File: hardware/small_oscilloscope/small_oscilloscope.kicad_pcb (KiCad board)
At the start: 2 copper layers, 98 parts, among them J1 Conn_01x16, J2 Conn_01x16, J3 Conn_Coaxial, J4 Conn_Coaxial, J5 Parellel LCD, J6 Conn_01x02, Q1 NTR5103NT1G, Q2 NTR5103NT1G, Q3 NTR5103NT1G, Q4 NTR5103NT1G, Q5 NTR5103NT1G, Q6 NTR5103NT1G, Q7 NTR5103NT1G, Q8 NTR5103NT1G, Q9 NTR5103NT1G, SW1 SW_MEC_5E, SW2 RotaryEncoder_Switch_MP, SW3 SW_MEC_5E, SW4 SW_MEC_5E, SW5 SW_MEC_5E, SW6 RotaryEncoder_Switch_MP, U1 CH423S, U10 EA2208T6R, U11 FT800Q-T, U12 LM358, U2 TMUX1101DBV, U3 TMUX1101DBV, U4 TMUX1101DBV, U5 TMUX1101DBV, U6 TL084, U7 LM311, U8 LM311, U9 NE555P, Y1 12.0000M

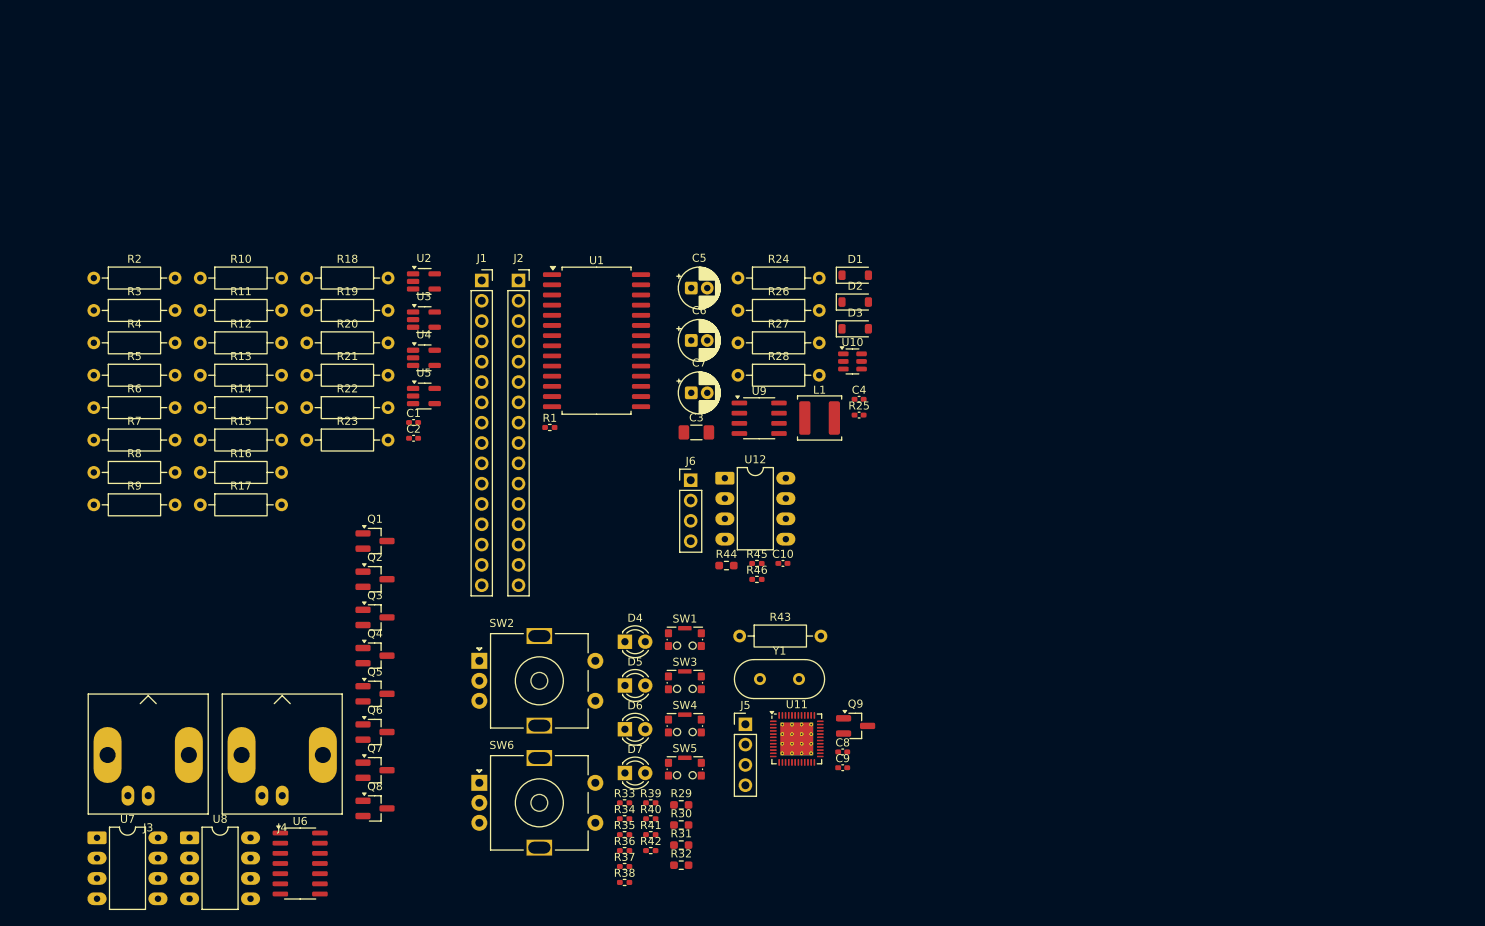
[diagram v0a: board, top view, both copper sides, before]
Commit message: feat: 오실로스코프 회로 설계 업데이트
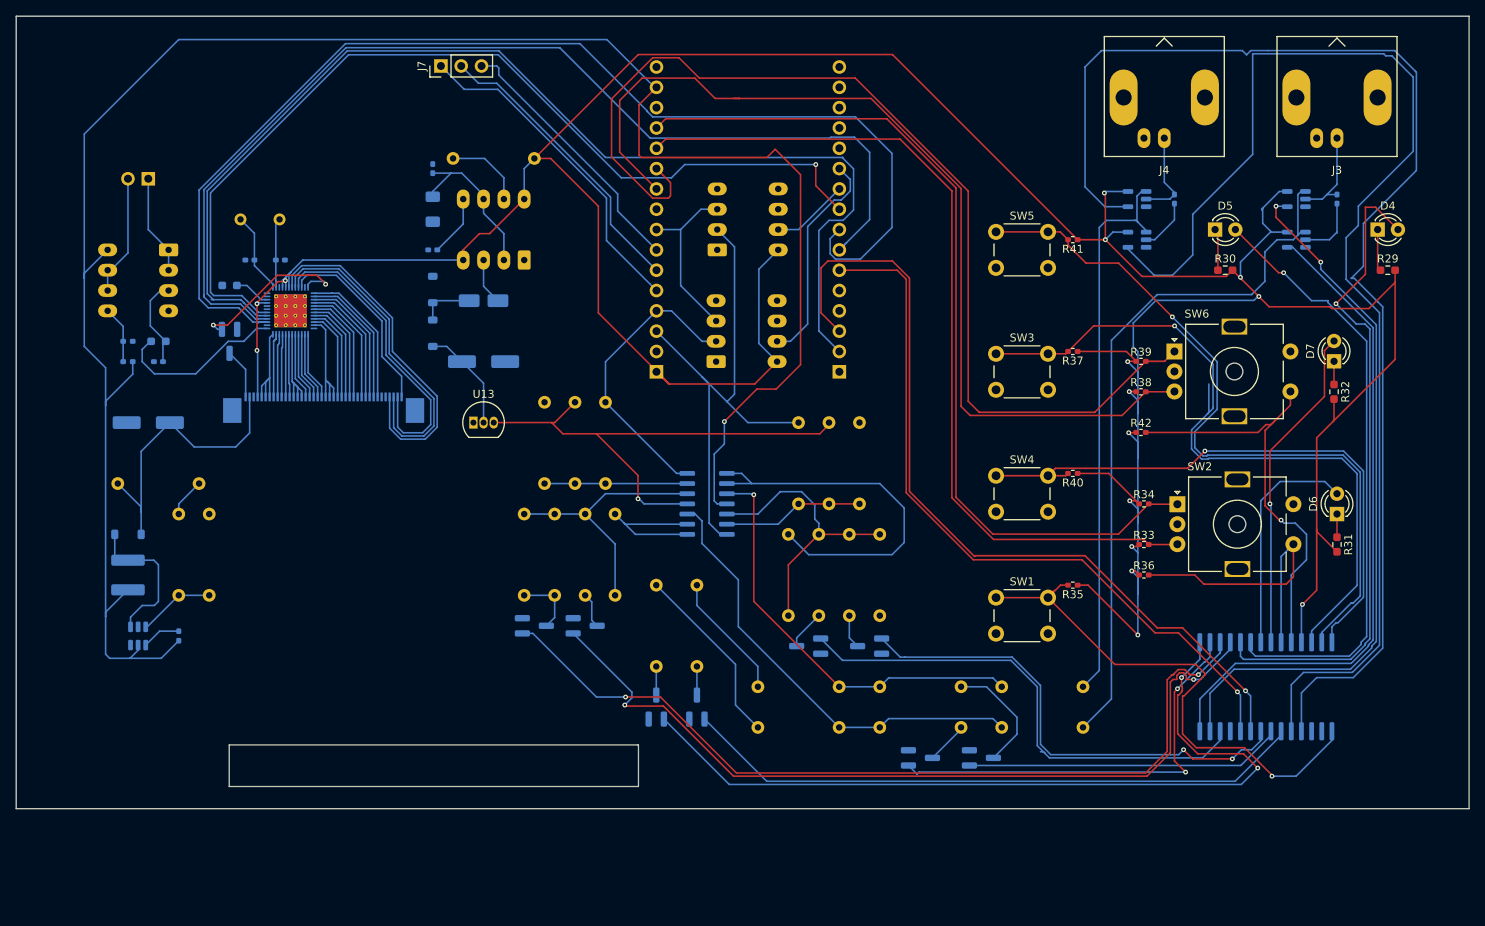
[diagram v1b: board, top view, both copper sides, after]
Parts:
- added J7: Conn_01x03, Connector_PinHeader_2.54mm:PinHeader_1x03_P2.54mm_Vertical, F.Cu at (124.2, 41.8)
- added U13: L79L05_TO92, Package_TO_SOT_THT:TO-92_Inline, F.Cu at (128.3, 86.4)
- C1, C10, C2, C3, C4, C8, C9, D1, D2, D3, J1, J2, L1, Q1, Q2, Q3, Q4, Q5, Q6, Q7, Q8, Q9, R1, R10, R11, R12, R13, R14, R15, R16, R17, R18, R19, R2, R20, R21, R22, R23, R24, R25, R26, R27, R28, R3, R4, R44, R45, R46, R5, R6, R7, R8, R9, U1, U10, U11, U12, U6, U7, U8, Y1: moved to B.Cu
- C5: footprint Capacitor_THT:CP_Radial_D5.0mm_P2.00mm -> Capacitor_SMD:CP_Elec_4x5.7; moved to B.Cu
- C6, C7: footprint Capacitor_THT:CP_Radial_D5.0mm_P2.00mm -> Capacitor_SMD:CP_Elec_6.3x5.7; moved to B.Cu
- J5: footprint Connector_PinHeader_2.54mm:PinHeader_1x04_P2.54mm_Vertical -> Connector_FFC-FPC:TE_4-1734839-0_1x40-1MP_P0.5mm_Horizontal; moved to B.Cu
- J6: footprint Connector_PinHeader_2.54mm:PinHeader_1x04_P2.54mm_Vertical -> Connector_PinHeader_2.54mm:PinHeader_1x02_P2.54mm_Vertical; moved to B.Cu
- R43: value 1K -> 1k; footprint Resistor_THT:R_Axial_DIN0207_L6.3mm_D2.5mm_P10.16mm_Horizontal -> Resistor_SMD:R_0603_1608Metric_Pad0.98x0.95mm_HandSolder; moved to B.Cu
- SW1, SW3, SW4, SW5: footprint Button_Switch_SMD:SW_SPST_CK_KMS2xxGP -> Button_Switch_THT:SW_PUSH_6mm_H4.3mm
- U2, U3, U4, U5: footprint Package_TO_SOT_SMD:SOT-23-5_HandSoldering -> Package_TO_SOT_SMD:SOT-23-5; moved to B.Cu
- U9: footprint Package_SO:SOIC-8_3.9x4.9mm_P1.27mm -> Package_DIP:DIP-8_W7.62mm_LongPads; moved to B.Cu
- moved J3 169.8 mm to (236.2, 50.8)
- moved J4 137.5 mm to (214.6, 50.8)
- moved R2 135.8 mm to (204.5, 124.5), turned to 180 degrees
- moved R4 130.9 mm to (204.5, 119.4), turned to 180 degrees
- moved C1 118.8 mm to (236.2, 58.4), turned to -90 degrees
- moved R3 111.2 mm to (179.1, 124.5)
- moved R29 110.8 mm to (242.6, 67.3)
- moved U3 110.1 mm to (231.1, 58.4), turned to 180 degrees
- moved U2 109.2 mm to (231.1, 63.5), turned to 180 degrees
- moved D4 107.3 mm to (241.3, 62.2)
- moved U7 106.8 mm to (158.8, 64.8)
- moved R5 105.7 mm to (179.1, 119.4)
- moved D7 102.5 mm to (235.8, 78.7), turned to 90 degrees
- moved SW6 102.3 mm to (215.9, 77.5)
- moved R6 101.4 mm to (174.0, 124.5), turned to 180 degrees
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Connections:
- C6 pad 2: -5V -> Net-(D2-A)
- D2 pad 2: -5V -> Net-(D2-A)
- J1 pad 5: unconnected-(J1-34-Pad5) -> Net-(J1-34)
- J1 pad 6: unconnected-(J1-32-Pad6) -> Net-(J1-32)
- J1 pad 7: unconnected-(J1-33-Pad7) -> Net-(J1-33)
- J5 pad 1: Net-(J5-LEDK) -> Net-(J5-YU)
- J5 pad 2: +24V -> Net-(J5-XL)
- J5 pad 3: GND -> Net-(J5-YD)
- J5 pad 4: +3.3V -> Net-(J5-XR)
- R21 pad 2: +5V -> -5V
- R23 pad 2: +5V -> -5V
- SW1 pad 2: /LCD UI/SW3 -> GND
- SW3 pad 2: /LCD UI/SW0 -> GND
- SW4 pad 2: /LCD UI/SW2 -> GND
- SW5 pad 2: /LCD UI/SW1 -> GND
- U10 pad 6: (no net) -> unconnected-(U10-NC-Pad6)
- U11 pad 49: (no net) -> GND
- U11 pad 6: /CS -> /SS
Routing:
- net +3.3V: track 0.00 -> 454.2 mm, vias 0 -> 15
- net +5V: track 0.00 -> 253.7 mm, vias 0 -> 1
- net /Q1: track 0.00 -> 159.5 mm
- net /Q2: track 0.00 -> 155.4 mm
- net /SCK: track 0.00 -> 146.8 mm
- net /MOSI: track 0.00 -> 142.7 mm
- net /MISO: track 0.00 -> 132.5 mm
- net /RE1A: track 0.00 -> 130.4 mm
- net /RE1B: track 0.00 -> 118.9 mm
- net /SS: track 0.00 -> 117.2 mm, vias 0 -> 1
- net /RE0A: track 0.00 -> 111.3 mm
- net /RE0B: track 0.00 -> 109.1 mm
- net /Q11: track 0.00 -> 107.8 mm, vias 0 -> 2
- net /SCL: track 0.00 -> 105.6 mm, vias 0 -> 1
- net /Q12: track 0.00 -> 105.5 mm, vias 0 -> 2
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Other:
- board outline added: 181.6 x 99.1 mm
- board text added: "480 x 272 Monitor"

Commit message: chore: KiCad 프로젝트 백업 파일 정리 및 PCB 파일 업데이트
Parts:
- U13: moved to B.Cu
- moved U13 2.54 mm to (130.8, 86.4), turned to 180 degrees
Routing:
- net GND: track 0.00 -> 46.1 mm, vias 0 -> 24
- net -5V: track 63.8 -> 67.8 mm
- net /LCD UI/SW0: track 91.5 -> 87.7 mm
- net Net-(Q8-D): track 4.24 -> 8.05 mm
- net Net-(U9-DIS): track 10.0 -> 12.8 mm
- net /LCD UI/SW3: track 67.2 -> 65.9 mm
- net /RE1B: track 118.9 -> 118.1 mm
- net /Q6: track 63.1 -> 62.5 mm
- added copper zone on B.Cu, net GND
- added copper zone on F.Cu, net GND

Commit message: feat: 소형 오실로스코프 하드웨어 개발 완료
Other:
- board text added: "4Ohm 3W"
- board text added: "LED0"
- board text added: "LED1"
- board text added: "LINE 0"
- board text added: "LINE 1"
- board text added: "LOLIN D32"
- board text added: "SPEAKER"
- board text added: "Time"
- board text added: "Voltage"
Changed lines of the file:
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@@
 			(outputformat 1)
 			(mirror no)
-			(drillshape 1)
+			(drillshape 0)
 			(scaleselection 1)
-			(outputdirectory "")
+			(outputdirectory "./gerber/")
 		)
 	)
@@
 	)
 	(gr_rect
+		(start 80.75 58.5)
+		(end 186.15 125.65)
+		(stroke
+			(width 0.1)
+			(type default)
+		)
+		(fill no)
+		(layer "F.Mask")
+	)
+	(gr_rect
 		(start 99.15 86.8)
 		(end 119.7 114.8)
@@
 		)
 		(fill no)
-		(layer "F.Mask")
+		(layer "B.Mask")
 	)
 	(gr_rect
@@
 		)
 		(fill no)
-		(layer "F.Mask")
+		(layer "B.Mask")
 	)
 	(gr_rect
-		(start 80.75 58.5)
-		(end 186.15 125.65)
+		(start 148.59 36.068)
+		(end 176.911 84.328)
 		(stroke
 			(width 0.1)
@@
 		)
 		(fill no)
-		(layer "F.Mask")
+		(layer "B.SilkS")
 	)
 	(gr_rect
@@
 		)
 	)
+	(gr_text "Time"
+		(at 221.996 91.059 0)
+		(layer "F.SilkS")
+		(effects
+			(font
+				(size 1 1)
+				(thickness 0.1)
+			)
+			(justify left bottom)
+		)
+	)
+	(gr_text "LINE 0"
+		(at 214.503 57.658 0)
+		(layer "F.SilkS")
+		(effects
+			(font
+				(size 1 1)
+				(thickness 0.1)
+			)
+			(justify bottom)
+		)
+	)
+	(gr_text "SPEAKER"
+		(at 83.312 52.832 0)
+		(layer "F.SilkS")
+		(effects
+			(font
+				(size 1 1)
+				(thickness 0.1)
+			)
+			(justify left bottom)
+		)
+	)
+	(gr_text "4Ohm 3W"
+		(at 82.804 50.546 0)
+		(layer "F.SilkS")
+		(effects
+			(font
+				(size 1 1)
+				(thickness 0.1)
+			)
+			(justify left bottom)
+		)
+	)
+	(gr_text "LINE 1"
+		(at 234.823 57.531 0)
+		(layer "F.SilkS")
+		(effects
+			(font
+				(size 1 1)
+				(thickness 0.1)
+			)
+			(justify left bottom)
+		)
+	)
+	(gr_text "LED1"
+		(at 215.265 62.992 0)
+		(layer "F.SilkS")
+		(effects
+			(font
+				(size 1 1)
+				(thickness 0.1)
+			)
+			(justify left bottom)
+		)
+	)
+	(gr_text "Voltage"
+		(at 220.853 72.009 0)
+		(layer "F.SilkS")
+		(effects
+			(font
+				(size 1 1)
+				(thickness 0.1)
+			)
+			(justify left bottom)
+		)
+	)
+	(gr_text "LED0"
+		(at 235.712 63.31 0)
+		(layer "F.SilkS")
+		(effects
+			(font
+				(size 1 1)
+				(thickness 0.1)
+			)
+			(justify left bottom)
+		)
+	)
+	(gr_text "LOLIN D32"
+		(at 166.624 38.862 0)
+		(layer "B.SilkS")
+		(effects
+			(font
+				(size 1 1)
+				(thickness 0.1)
+			)
+			(justify left bottom mirror)
+		)
+	)
 	(segment
 		(start 232.49 63.5)
@@
 	)
 	(segment
-		(start 109.093 74.803)
-		(end 109.22 74.93)
-		(width 0.2)
-		(layer "B.Cu")
-		(net 6)
-	)
-	(segment
-		(start 107.7439 68.346)
+		(start 107.676 68.346)
 		(end 110.256 68.346)
 		(width 0.2)
@@
 	)
 	(segment
-		(start 107.21 68.812)
-		(end 107.569 68.453)
-		(width 0.2)
-		(layer "B.Cu")
-		(net 6)
-	)
-	(segment
 		(start 88.3325 78.0455)
 		(end 87.884 77.597)
@@
 	)
 	(segment
-		(start 107.676 68.346)
-		(end 107.7439 68.346)
-		(width 0.2)
-		(layer "B.Cu")
-		(net 6)
-	)
-	(segment
 		(start 86.36 111.8925)
 		(end 86.36 111.230001)
@@
 	)
 	(segment
-		(start 101.6853 74.19)
-		(end 101.578 74.19)
-		(width 0.2)
-		(layer "B.Cu")
-		(net 6)
-	)
-	(segment
 		(start 100.8 83.15)
 		(end 100.8 85.179)
@@
 	)
 	(segment
-		(start 107.569 68.453)
+		(start 107.21 68.812)
 		(end 107.676 68.346)
 		(width 0.2)
@@
 	)
 	(segment
-		(start 102.4725 74.19)
-		(end 101.6853 74.19)
+		(start 101.578 74.19)
+		(end 102.4725 74.19)
 		(width 0.2)
 		(layer "B.Cu")
@@
 	)
 	(segment
-		(start 101.6853 74.19)
-		(end 101.854 74.19)
-		(width 0.2)
-		(layer "B.Cu")
-		(net 6)
-	)
-	(segment
 		(start 109.22 74.93)
 		(end 109.22 75.565)
@@
 	(segment
 		(start 108.88 74.59)
-		(end 109.093 74.803)
+		(end 109.22 74.93)
 		(width 0.2)
 		(layer "B.Cu")
@@
 	)
 	(segment
-		(start 237.363 68.453)
-		(end 237.363 64.778767)
-		(width 0.2)
-		(layer "B.Cu")
-		(net 101)
-	)
-	(segment
 		(start 242.316 40.513)
 		(end 242.062 40.259)
@@
 	)
 	(segment
-		(start 237.363 64.652498)
-		(end 237.363 60.833)
-		(width 0.2)
-		(layer "B.Cu")
-		(net 101)
-	)
-	(segment
 		(start 237.363 60.833)
 		(end 245.745 52.451)
@@
 	)
 	(segment
-		(start 237.363 64.778767)
-		(end 237.363 64.652498)
+		(start 237.363 68.453)
+		(end 237.363 60.833)
 		(width 0.2)
 		(layer "B.Cu")

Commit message: board edit
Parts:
- added REF**: TestPoint_Plated_Hole_D3.0mm, TestPoint:TestPoint_Plated_Hole_D3.0mm, F.Cu at (248.0, 41.0)
- added REF**: TestPoint_Plated_Hole_D3.0mm, TestPoint:TestPoint_Plated_Hole_D3.0mm, F.Cu at (77.0, 41.0)
- added REF**: TestPoint_Plated_Hole_D3.0mm, TestPoint:TestPoint_Plated_Hole_D3.0mm, F.Cu at (77.0, 129.0)
- added REF**: TestPoint_Plated_Hole_D3.0mm, TestPoint:TestPoint_Plated_Hole_D3.0mm, F.Cu at (248.0, 129.0)
- U11: footprint Package_DFN_QFN:VQFN-48-1EP_6x6mm_P0.4mm_EP4.1x4.1mm_ThermalVias -> Package_DFN_QFN:VQFN-48-1EP_7x7mm_P0.5mm_EP4.1x4.1mm
- moved D6 2.79 mm to (236.2, 95.0), turned to -90 degrees
- moved D5 2.54 mm to (223.5, 62.2), turned to 180 degrees
- moved D4 2.54 mm to (243.8, 62.2), turned to 180 degrees
- moved D7 2.50 mm to (235.8, 76.2), turned to -90 degrees
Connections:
- D4 pad 1: Net-(D4-K) -> /LCD UI/LED0
- D4 pad 2: /LCD UI/LED0 -> Net-(D4-A)
- D5 pad 1: Net-(D5-K) -> /LCD UI/LED1
- D5 pad 2: /LCD UI/LED1 -> Net-(D5-A)
- D6 pad 1: Net-(D6-K) -> /LCD UI/LEDRE0
- D6 pad 2: /LCD UI/LEDRE0 -> Net-(D6-A)
- D7 pad 1: Net-(D7-K) -> /LCD UI/LEDRE1
- D7 pad 2: /LCD UI/LEDRE1 -> Net-(D7-A)
- R29 pad 1: Net-(D4-K) -> Net-(D4-A)
- R30 pad 1: Net-(D5-K) -> Net-(D5-A)
- R31 pad 1: Net-(D6-K) -> Net-(D6-A)
- R32 pad 1: Net-(D7-K) -> Net-(D7-A)
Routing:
- net Net-(D5-K): track 5.23 -> 0.00 mm
- net Net-(D5-A): track 0.00 -> 5.23 mm
- net Net-(D4-K): track 5.23 -> 0.00 mm
- net Net-(D4-A): track 0.00 -> 5.23 mm
- net Net-(D7-K): track 2.90 -> 0.00 mm
- net Net-(D7-A): track 0.00 -> 2.90 mm
- net Net-(D6-K): track 2.90 -> 0.00 mm
- net Net-(D6-A): track 0.00 -> 2.90 mm
- net GND: track 46.0 -> 43.5 mm
- net /SCK: track 146.6 -> 145.2 mm
- net Net-(J5-R3): track 8.44 -> 7.38 mm
- net Net-(J5-R0): track 13.2 -> 12.3 mm
- net Net-(J5-G0): track 12.3 -> 11.5 mm
- net /Q1: track 159.2 -> 158.4 mm
- net Net-(J5-G7): track 8.52 -> 7.79 mm
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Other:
- outline, holes or cut-outs redrawn
- board text added: "Small Oscilliscope made by Giho Park"

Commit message: oscilliscope first success
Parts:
- removed the C3 at (123.2, 59.7)
- removed the C4 at (123.2, 64.8)
- removed the C6 at (129.5, 78.7)
- removed the D2 at (123.2, 75.2)
- removed the J2 at (174.0, 80.0)
- removed the Q9 at (97.8, 76.2)
- removed the R25 at (123.2, 54.6)
- removed the R27 at (91.4, 97.8)
- removed the REF** at (248.0, 41.0)
- removed the REF** at (77.0, 41.0)
- removed the REF** at (77.0, 129.0)
- removed the REF** at (248.0, 129.0)
- removed the U13 at (130.8, 86.4)
- removed the U3 at (231.1, 58.4)
- removed the U4 at (211.2, 63.5)
- removed the U5 at (211.2, 58.4)
- added AE1: Antenna_Chip, Inductor_SMD:L_1206_3216Metric_Pad1.22x1.90mm_HandSolder, B.Cu at (173.7, 130.4)
- added C1: 10u, Capacitor_SMD:CP_Elec_5x5.3, B.Cu at (161.3, 104.4)
- added C10: 10u, Capacitor_SMD:CP_Elec_6.3x5.7, B.Cu at (146.3, 99.6)
- added C13: 10u, Capacitor_SMD:CP_Elec_5x5.3, B.Cu at (110.0, 63.5)
- added C2: 0.1u, Capacitor_SMD:C_0402_1005Metric_Pad0.74x0.62mm_HandSolder, B.Cu at (179.4, 115.8)
- added C7: 47u, Capacitor_SMD:CP_Elec_5x5.3, B.Cu at (140.5, 105.4)
- added C8: 100u, Capacitor_SMD:CP_Elec_5x5.3, B.Cu at (128.5, 104.6)
- added C9: 47u, Capacitor_SMD:CP_Elec_6.3x5.7, B.Cu at (135.4, 98.3)
- added D12: LED, LED_THT:LED_D3.0mm, F.Cu at (115.2, 47.0)
- added D3: 1N5819, Diode_SMD:D_SOD-123, B.Cu at (142.0, 93.5)
- added D4: LED_Small, LED_THT:LED_D3.0mm, F.Cu at (99.7, 47.0)
- added D5: LED_Small, LED_THT:LED_D3.0mm, F.Cu at (107.6, 47.0)
- added D6: 1N5819, Diode_SMD:D_SOD-123, B.Cu at (130.3, 91.2)
- added D7: 1N5819, Diode_SMD:D_SOD-123, B.Cu at (148.1, 69.1)
- added J4: BAT, Connector_PinSocket_2.54mm:PinSocket_1x02_P2.54mm_Vertical, F.Cu at (79.3, 50.3)
- added K1: FINDER-40.41, Relay_THT:Relay_SPDT_Finder_40.41, F.Cu at (205.9, 81.5)
- added K2: FINDER-40.41, Relay_THT:Relay_SPDT_Finder_40.41, F.Cu at (233.2, 81.5)
- added K3: FINDER-40.41, Relay_THT:Relay_SPDT_Finder_40.41, F.Cu at (219.5, 81.5)
- added K4: FINDER-40.41, Relay_THT:Relay_SPDT_Finder_40.41, F.Cu at (233.2, 120.6)
- added L2: 10u, Inductor_SMD:L_7.3x7.3_H3.5, B.Cu at (140.2, 86.4)
- added L3: 10u, Inductor_SMD:L_7.3x7.3_H3.5, B.Cu at (129.8, 85.1)
- added L4: 10u, Inductor_SMD:L_7.3x7.3_H3.5, B.Cu at (136.4, 75.7)
- added L5: 100u, Inductor_SMD:L_7.3x7.3_H3.5, B.Cu at (149.9, 75.4)
- added Q1: 2SC4671, Package_TO_SOT_SMD:SOT-523, B.Cu at (88.8, 47.5)
- added Q12: 2SC4671, Package_TO_SOT_SMD:SOT-523, F.Cu at (233.7, 125.5)
- added Q13: 2SC4671, Package_TO_SOT_SMD:SOT-523, B.Cu at (91.3, 116.8)
- added Q14: 2SC4671, Package_TO_SOT_SMD:SOT-523, F.Cu at (119.4, 51.7)
- added Q15: 2SC4671, Package_TO_SOT_SMD:SOT-523, F.Cu at (119.4, 54.9)
- added Q7: 2SC4671, Package_TO_SOT_SMD:SOT-523, F.Cu at (235.3, 90.8)
- added Q8: 2SC4671, Package_TO_SOT_SMD:SOT-523, F.Cu at (222.8, 90.7)
- added R10: 10k, Resistor_SMD:R_0402_1005Metric_Pad0.72x0.64mm_HandSolder, B.Cu at (85.5, 45.5)
- added R11: 10k, Resistor_SMD:R_0402_1005Metric_Pad0.72x0.64mm_HandSolder, B.Cu at (85.5, 50.3)
- added R12: 10K, Resistor_SMD:R_0402_1005Metric_Pad0.72x0.64mm_HandSolder, B.Cu at (156.2, 109.2)
- added R13: 100, Resistor_SMD:R_0603_1608Metric_Pad0.98x0.95mm_HandSolder, B.Cu at (152.4, 106.7)
- added R14: 10K, Resistor_SMD:R_0402_1005Metric_Pad0.72x0.64mm_HandSolder, B.Cu at (149.9, 113.3)
- added R15: 10K, Resistor_SMD:R_0402_1005Metric_Pad0.72x0.64mm_HandSolder, B.Cu at (149.9, 111.8)
- added R16: 4K7, Resistor_SMD:R_0402_1005Metric_Pad0.72x0.64mm_HandSolder, B.Cu at (149.9, 109.0)
- added R17: 10K, Resistor_SMD:R_0402_1005Metric_Pad0.72x0.64mm_HandSolder, B.Cu at (149.9, 110.2)
- added R18: 10K, Resistor_SMD:R_0402_1005Metric_Pad0.72x0.64mm_HandSolder, B.Cu at (152.7, 113.3)
- added R19: 3K, Resistor_SMD:R_0402_1005Metric_Pad0.72x0.64mm_HandSolder, B.Cu at (152.7, 111.8)
- added R2: 10k, Resistor_SMD:R_0402_1005Metric_Pad0.72x0.64mm_HandSolder, B.Cu at (187.2, 125.1)
- added R20: 820R, Resistor_SMD:R_0402_1005Metric_Pad0.72x0.64mm_HandSolder, B.Cu at (152.7, 109.0)
- added R22: 10K, Resistor_SMD:R_0402_1005Metric_Pad0.72x0.64mm_HandSolder, B.Cu at (158.8, 109.2)
- added R23: 1k, Resistor_SMD:R_0603_1608Metric_Pad0.98x0.95mm_HandSolder, F.Cu at (139.3, 45.7)
- added R3: 10k, Resistor_SMD:R_0402_1005Metric_Pad0.72x0.64mm_HandSolder, B.Cu at (170.2, 121.8)
- added R33: 3k, Resistor_SMD:R_0402_1005Metric_Pad0.72x0.64mm_HandSolder, F.Cu at (201.5, 86.4)
- added R35: 3K6, Resistor_THT:R_Axial_DIN0207_L6.3mm_D2.5mm_P10.16mm_Horizontal, B.Cu at (175.0, 63.8)
- added R38: 3k, Resistor_SMD:R_0402_1005Metric_Pad0.72x0.64mm_HandSolder, F.Cu at (232.2, 90.9)
- added R4: 10k, Resistor_SMD:R_0402_1005Metric_Pad0.72x0.64mm_HandSolder, B.Cu at (163.7, 113.3)
- added R42: 3K6, Resistor_THT:R_Axial_DIN0207_L6.3mm_D2.5mm_P10.16mm_Horizontal, B.Cu at (159.0, 65.9)
- added R43: 3K6, Resistor_THT:R_Axial_DIN0207_L6.3mm_D2.5mm_P10.16mm_Horizontal, B.Cu at (155.2, 65.9)
- added R5: 10k, Resistor_SMD:R_0402_1005Metric_Pad0.72x0.64mm_HandSolder, B.Cu at (169.3, 107.2)
- added R51: 3k, Resistor_SMD:R_0402_1005Metric_Pad0.72x0.64mm_HandSolder, F.Cu at (220.5, 90.7)
- added R52: 3k, Resistor_SMD:R_0402_1005Metric_Pad0.72x0.64mm_HandSolder, F.Cu at (231.0, 125.6)
- added R54: 10k, Resistor_SMD:R_0402_1005Metric_Pad0.72x0.64mm_HandSolder, B.Cu at (88.0, 119.9)
- added R56: 10k, Resistor_SMD:R_0402_1005Metric_Pad0.72x0.64mm_HandSolder, B.Cu at (90.8, 120.1)
- added R57: 147k, Resistor_SMD:R_0402_1005Metric_Pad0.72x0.64mm_HandSolder, B.Cu at (142.2, 80.5)
- added R58: 1k, Resistor_SMD:R_0603_1608Metric_Pad0.98x0.95mm_HandSolder, F.Cu at (101.2, 51.6)
- added R59: 1k, Resistor_SMD:R_0603_1608Metric_Pad0.98x0.95mm_HandSolder, F.Cu at (109.1, 51.6)
- added R6: 10k, Resistor_SMD:R_0402_1005Metric_Pad0.72x0.64mm_HandSolder, B.Cu at (169.3, 108.5)
- added R60: 7.5k, Resistor_SMD:R_1206_3216Metric_Pad1.30x1.75mm_HandSolder, B.Cu at (142.5, 71.1)
- added R61: 1k, Resistor_SMD:R_0603_1608Metric_Pad0.98x0.95mm_HandSolder, F.Cu at (85.8, 45.2)
- added R62: 22k, Resistor_SMD:R_1206_3216Metric_Pad1.30x1.75mm_HandSolder, B.Cu at (124.2, 74.2)
- added R63: 470k, Resistor_SMD:R_0402_1005Metric_Pad0.72x0.64mm_HandSolder, B.Cu at (136.9, 62.5)
- added R64: 3k, Resistor_SMD:R_0402_1005Metric_Pad0.72x0.64mm_HandSolder, B.Cu at (124.5, 68.6)
- added R65: 100k, Resistor_SMD:R_0402_1005Metric_Pad0.72x0.64mm_HandSolder, B.Cu at (133.6, 62.5)
- added R7: 10k, Resistor_SMD:R_0402_1005Metric_Pad0.72x0.64mm_HandSolder, B.Cu at (173.5, 107.6)
- added R8: 10k, Resistor_SMD:R_0402_1005Metric_Pad0.72x0.64mm_HandSolder, B.Cu at (85.5, 48.0)
- added R80: 150, Resistor_SMD:R_0402_1005Metric_Pad0.72x0.64mm_HandSolder, B.Cu at (94.2, 79.8)
- added R81: 10k, Resistor_SMD:R_0402_1005Metric_Pad0.72x0.64mm_HandSolder, B.Cu at (93.0, 74.2)
- added R82: 10k, Resistor_SMD:R_0402_1005Metric_Pad0.72x0.64mm_HandSolder, B.Cu at (94.2, 70.1)
- added R83: 10R, Resistor_SMD:R_1206_3216Metric_Pad1.30x1.75mm_HandSolder, B.Cu at (87.4, 77.2)
- added R84: 10R, Resistor_SMD:R_1206_3216Metric_Pad1.30x1.75mm_HandSolder, B.Cu at (87.4, 74.4)
- added R85: 10R, Resistor_SMD:R_1206_3216Metric_Pad1.30x1.75mm_HandSolder, B.Cu at (87.4, 71.9)
- added R86: 10R, Resistor_SMD:R_1206_3216Metric_Pad1.30x1.75mm_HandSolder, B.Cu at (94.0, 75.9)
- added R87: 10R, Resistor_SMD:R_1206_3216Metric_Pad1.30x1.75mm_HandSolder, B.Cu at (94.0, 72.1)
- added R9: 10k, Resistor_SMD:R_0402_1005Metric_Pad0.72x0.64mm_HandSolder, B.Cu at (85.5, 52.8)
- added R93: 3k, Resistor_SMD:R_0402_1005Metric_Pad0.72x0.64mm_HandSolder, F.Cu at (116.6, 51.6)
- added R94: 10k, Resistor_SMD:R_0402_1005Metric_Pad0.72x0.64mm_HandSolder, F.Cu at (123.3, 54.2)
- added R95: 10k, Resistor_SMD:R_0402_1005Metric_Pad0.72x0.64mm_HandSolder, F.Cu at (123.3, 52.5)
- added REF**: TestPoint_Loop_D3.80mm_Drill2.8mm, TestPoint:TestPoint_Loop_D3.80mm_Drill2.8mm, F.Cu at (245.0, 44.0)
- added REF**: TestPoint_Loop_D3.80mm_Drill2.8mm, TestPoint:TestPoint_Loop_D3.80mm_Drill2.8mm, F.Cu at (245.0, 134.0)
- added REF**: TestPoint_Loop_D3.80mm_Drill2.8mm, TestPoint:TestPoint_Loop_D3.80mm_Drill2.8mm, F.Cu at (77.0, 134.0)
- added REF**: TestPoint_Loop_D3.80mm_Drill2.8mm, TestPoint:TestPoint_Loop_D3.80mm_Drill2.8mm, F.Cu at (77.0, 44.0)
- added U10: EA8105, Package_TO_SOT_SMD:SOT-23-6, B.Cu at (136.4, 66.0)
- added U11: LM2576S-12, Package_TO_SOT_SMD:TO-263-5_TabPin3, B.Cu at (145.5, 55.0)
- added U14: CH340C, Package_SO:SOIC-16_3.9x9.9mm_P1.27mm, F.Cu at (132.3, 54.5)
- added U7: EA2208T6R, Package_TO_SOT_SMD:SOT-23-6, B.Cu at (142.7, 76.5)
- added U8: TP4056-42-ESOP8, Package_SO:SOIC-8-1EP_3.9x4.9mm_P1.27mm_EP2.41x3.3mm_ThermalVias, F.Cu at (92.7, 47.8)
- C5: value 10u -> 100u; footprint Capacitor_SMD:CP_Elec_4x5.7 -> Capacitor_SMD:CP_Elec_5x5.3
- C6: renamed from C7; value 47u -> 10u; footprint Capacitor_SMD:CP_Elec_6.3x5.7 -> Capacitor_SMD:CP_Elec_5x5.3
- D1: value D_Schottky -> 1N5225B; footprint Diode_SMD:D_SOD-123 -> Diode_THT:D_A-405_P7.62mm_Horizontal
- J1: value Conn_01x16 -> SIGNAL; footprint Connector_PinSocket_2.54mm:PinSocket_1x16_P2.54mm_Vertical -> Connector_PinSocket_2.54mm:PinSocket_1x02_P2.54mm_Vertical
- J6: value Conn_01x02 -> SPEAKER; footprint Connector_PinHeader_2.54mm:PinHeader_1x02_P2.54mm_Vertical -> Connector_PinSocket_2.54mm:PinSocket_1x02_P2.54mm_Vertical
- J7: value Conn_01x03 -> USB_B_Mini; footprint Connector_PinHeader_2.54mm:PinHeader_1x03_P2.54mm_Vertical -> Connector_USB:USB_Mini-B_Lumberg_2486_01_Horizontal
- L1: value 1u -> 10u; footprint Inductor_SMD:L_Changjiang_FNR5045S -> Inductor_SMD:L_7.3x7.3_H3.5
- Q10: renamed from Q5; value NTR5103NT1G -> BSS138
- Q11: renamed from Q7; value NTR5103NT1G -> BSS138
- Q2: value NTR5103NT1G -> 2SC4671; footprint Package_TO_SOT_SMD:SOT-23_Handsoldering -> Package_TO_SOT_SMD:SOT-523
- Q3: value NTR5103NT1G -> 2SC4671; footprint Package_TO_SOT_SMD:SOT-23_Handsoldering -> Package_TO_SOT_SMD:SOT-523; moved to F.Cu
- Q4: value NTR5103NT1G -> BSS138; moved to F.Cu
- Q5: renamed from Q6; value NTR5103NT1G -> BSS138
- Q6: renamed from Q8; value NTR5103NT1G -> BSS138
- Q9: renamed from Q1; value NTR5103NT1G -> BSS138; moved to F.Cu
- R21: value 3K -> 10K; footprint Resistor_THT:R_Axial_DIN0207_L6.3mm_D2.5mm_P10.16mm_Horizontal -> Resistor_SMD:R_0402_1005Metric_Pad0.72x0.64mm_HandSolder
- R24: value 560 -> 1k; footprint Resistor_THT:R_Axial_DIN0207_L6.3mm_D2.5mm_P10.16mm_Horizontal -> Resistor_SMD:R_0603_1608Metric_Pad0.98x0.95mm_HandSolder; moved to F.Cu
- R27: renamed from R5; moved to F.Cu
- R30: renamed from R15; value 500 -> 500R
- R31: renamed from R17; value 500 -> 500R
- R36: renamed from R23; value 3K -> 3K6
- R37: renamed from R19; value 150 -> 150R
- R44: renamed from R3; moved to F.Cu
- R47: renamed from R14; value 500 -> 500R
- R48: renamed from R16; value 500 -> 500R
- R49: renamed from R18; value 150 -> 150R
- R53: renamed from R26; value 10k -> 4.7k; footprint Resistor_THT:R_Axial_DIN0207_L6.3mm_D2.5mm_P10.16mm_Horizontal -> Resistor_SMD:R_0402_1005Metric_Pad0.72x0.64mm_HandSolder
- R55: renamed from R28; value 500 -> 120; footprint Resistor_THT:R_Axial_DIN0207_L6.3mm_D2.5mm_P10.16mm_Horizontal -> Resistor_SMD:R_0402_1005Metric_Pad0.72x0.64mm_HandSolder
- R89: renamed from R43; value 1k -> 10k; footprint Resistor_SMD:R_0603_1608Metric_Pad0.98x0.95mm_HandSolder -> Resistor_SMD:R_0402_1005Metric_Pad0.72x0.64mm_HandSolder
- U1: moved to F.Cu
- U13: renamed from U12; footprint Package_DIP:DIP-8_W7.62mm_LongPads -> Package_SO:SOIC-8_3.9x4.9mm_P1.27mm
- U2: value TMUX1101DBV -> ESP32-PICO-D4; footprint Package_TO_SOT_SMD:SOT-23-5 -> Package_DFN_QFN:QFN-48-1EP_7x7mm_P0.5mm_EP5.3x5.3mm
- U4: renamed from U7; moved to F.Cu
- U5: renamed from U8; moved to F.Cu
- U9: value NE555P -> EA2208T6R; footprint Package_DIP:DIP-8_W7.62mm_LongPads -> Package_TO_SOT_SMD:SOT-23-6
- moved Q2 128.4 mm to (88.8, 51.6), turned to 180 degrees
- moved Q4 98.4 mm to (245.4, 80.3)
- moved R1 96.8 mm to (187.2, 127.3), turned to 180 degrees
- moved R50 91.0 mm to (242.1, 109.3), turned to 180 degrees
- moved R27 85.4 mm to (245.1, 65.3), turned to -90 degrees
- moved R28 84.0 mm to (242.0, 70.2)
- moved R32 81.9 mm to (231.6, 74.7), turned to 0 degrees
- moved U2 79.0 mm to (171.4, 115.3), turned to 90 degrees
- moved R45 69.1 mm to (242.1, 112.8)
- moved R44 69.0 mm to (245.4, 105.2), turned to -90 degrees
- moved Q3 63.5 mm to (203.8, 86.4), turned to 0 degrees
- moved Q9 62.0 mm to (245.6, 120.4), turned to 90 degrees
- moved R39 56.0 mm to (218.1, 70.2), turned to 0 degrees
- moved J1 55.1 mm to (194.6, 46.0), turned to -90 degrees
- moved D1 53.1 mm to (156.2, 111.3)
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- renumbered C8 to C11, C9 to C12, C10 to C14, C2 to C3, C1 to C4, D6 to D10, D7 to D11, D3 to D2, D4 to D8, D5 to D9, J4 to J2, R4 to R25, R12 to R26, R8 to R28, R13 to R29, R9 to R32, R22 to R34, R2 to R39, R10 to R40, R20 to R41, R6 to R45, R11 to R46, R7 to R50, R40 to R66, R29 to R67, R30 to R68, R35 to R69, R37 to R70, R41 to R71, R31 to R72, R32 to R73, R36 to R74, R38 to R75, R39 to R76, R42 to R77, R33 to R78, R34 to R79, R44 to R90, R45 to R91, R46 to R92, SW4 to SW1, SW1 to SW2, SW5 to SW4, SW6 to SW5, SW2 to SW6, U11 to U12, U6 to U3, U10 to U6
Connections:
- C4 pad 2: Net-(C1-Pad2) -> Net-(C4-Pad2)
- C5 pad 1: Net-(U9-Q) -> Vbat
- C5 pad 2: Net-(D1-A) -> GND
- D1 pad 1: GND -> Net-(D1-K)
- D1 pad 2: Net-(D1-A) -> GND
- J1 pad 1: +3.3V -> /TESTPIN
- J1 pad 2: unconnected-(J1-RESET-Pad2) -> /TESTPIN
- J5 pad 39: +24V -> Net-(J5-LEDA)
- J5 pad 40: Net-(J5-LEDK) -> GND
- J5 pad 6: GND -> unconnected-(J5-NC-Pad6)
- J7 pad 1: Net-(J1-34) -> Vusb
- J7 pad 2: Net-(J1-32) -> Net-(J7-D-)
- J7 pad 3: Net-(J1-33) -> Net-(J7-D+)
- L1 pad 1: +5V -> Vbat
- Q2 pad 1: /Q4 -> Net-(Q2-B)
- Q2 pad 3: Net-(Q2-D) -> /~{STDBY}
- Q3 pad 1: /Q9 -> Net-(Q3-B)
- Q3 pad 3: Net-(Q3-D) -> Net-(Q3-C)
- Q4 pad 1: /Q3 -> /Q4
- R1 pad 1: +5V -> +3.3V
- R1 pad 2: /Power/BACKLIGHT -> /SCL
- R21 pad 1: Net-(U6D--) -> /VREF3V3
- R21 pad 2: -5V -> GND
- R24 pad 1: +3.3V -> /USB Serial/RXD
- R24 pad 2: Net-(U9-DIS) -> /TXD
- R25 pad 2: Net-(U6A-+) -> Net-(U3A-+)
- R27 pad 1: Net-(U6A-+) -> Net-(U3A-+)
- R27 pad 2: Net-(Q2-D) -> Net-(Q4-D)
- R28 pad 1: Net-(U6A-+) -> Net-(K2-Pad14)
- R32 pad 2: Net-(Q4-D) -> GND
- R34 pad 1: Net-(U6B--) -> Net-(U3B--)
- R36 pad 1: Net-(U6B--) -> Net-(R35-Pad2)
- R36 pad 2: -5V -> -12V
- R37 pad 1: Net-(U6B--) -> Net-(U3B--)
- R39 pad 1: Net-(R2-Pad1) -> Net-(K3-Pad11)
- R39 pad 2: Net-(U6C-+) -> Net-(U3C-+)
- R41 pad 1: Net-(U6D--) -> Net-(U3D--)
- R44 pad 1: Net-(U6C-+) -> Net-(U3C-+)
- R45 pad 1: Net-(U6C-+) -> Net-(K4-Pad14)
- R49 pad 1: Net-(U6D--) -> Net-(U3D--)
- R50 pad 2: Net-(Q3-D) -> GND
- R53 pad 2: Net-(R26-Pad2) -> Net-(U6-FB)
- R55 pad 1: Net-(U10-FB) -> Net-(U6-FB)
- R91 pad 1: +5V -> +3.3V
- U1 pad 14: /Q8 -> unconnected-(U1-OC7-Pad14)
- U1 pad 2: unconnected-(U1-IO6-Pad2) -> /~{STDBY}
- U1 pad 3: unconnected-(U1-IO7-Pad3) -> /~{CHRG}
- U1 pad 5: /Q2 -> /BACKLIGHT
- U12 pad 11: unconnected-(U11-INT_N-Pad11) -> Net-(U12-INT_N)
- U12 pad 12: unconnected-(U11-PD_N-Pad12) -> Net-(U12-PD_N)
- U12 pad 17: +3.3V -> Net-(U12-VCC1V2)
- U12 pad 24: Net-(Q9-G) -> unconnected-(U12-BACKLIGHT-Pad24)
- U12 pad 3: /SCK -> Net-(U12-SPI_SCLK/_I2C_SCL)
- U12 pad 4: /MISO -> Net-(U12-MISO/_I2C_SDA)
- U12 pad 5: /MOSI -> Net-(U12-MOSI/_I2C_SA0)
- U12 pad 6: /SS -> Net-(U12-CS_N/_I2C_SA1)
- U13 pad 8: +5V -> +3.3V
- U2 pad 1: Net-(R2-Pad1) -> +3.3V
- U2 pad 2: Net-(C1-Pad2) -> /ANT50R
- U2 pad 3: GND -> +3.3V
- U2 pad 4: /Q8 -> +3.3V
- U2 pad 5: +3.3V -> /VREFBAT
- U3 pad 10: Net-(U6C-+) -> Net-(U3C-+)
- U3 pad 11: -5V -> -12V
- U3 pad 13: Net-(U6D--) -> Net-(U3D--)
- U3 pad 3: Net-(U6A-+) -> Net-(U3A-+)
- U3 pad 4: +5V -> +12V
- U3 pad 6: Net-(U6B--) -> Net-(U3B--)
- U6 pad 3: Net-(U10-FB) -> Net-(U6-FB)
- U6 pad 4: /Power/BACKLIGHT -> Net-(Q13-C)
- U6 pad 5: +5V -> Vbat
- U9 pad 1: GND -> Net-(D6-A)
- U9 pad 2: Net-(U9-THR) -> GND
- U9 pad 3: Net-(U9-Q) -> Net-(U9-FB)
- U9 pad 4: +3.3V -> Vbat
- U9 pad 5: Net-(U9-CV) -> Vbat
- U9 pad 6: Net-(U9-THR) -> unconnected-(U9-NC-Pad6)
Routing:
- net GND: track 43.5 -> 372.7 mm, vias 24 -> 62
- net Vbat: track 0.00 -> 283.2 mm, vias 0 -> 7
- net /~{CHRG}: track 0.00 -> 221.8 mm, vias 0 -> 1
- net /~{STDBY}: track 0.00 -> 212.4 mm, vias 0 -> 1
- net /EN: track 0.00 -> 199.3 mm, vias 0 -> 3
- net /IO0: track 0.00 -> 198.6 mm, vias 0 -> 3
- net /Q2: track 154.7 -> 0.00 mm
- net /BACKLIGHT: track 0.00 -> 142.1 mm, vias 0 -> 1
- net Net-(U3C-+): track 0.00 -> 132.0 mm, vias 0 -> 2
- net /~{INT}: track 0.00 -> 121.5 mm, vias 0 -> 2
- net /TXD: track 0.00 -> 113.4 mm, vias 0 -> 1
- net /RXD: track 0.00 -> 111.1 mm, vias 0 -> 1
- net /TESTPIN: track 0.00 -> 106.0 mm, vias 0 -> 1
- net Net-(U3A-+): track 0.00 -> 105.0 mm, vias 0 -> 2
- net -12V: track 0.00 -> 97.4 mm
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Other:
- board size 181.6 x 99.1 mm -> 177 x 99 mm
- board text added: "+ -"
- board text added: "3.7V Li-Po"
- board text added: "Charging"
- board text added: "Complete"
- board text added: "Power"
- board text removed: "LOLIN D32"
